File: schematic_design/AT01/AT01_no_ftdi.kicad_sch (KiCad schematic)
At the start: 58 parts, among them J1 JST Connector, J2 Conn_01x08, J3 USB_C_Receptacle_USB2.0, J4 DC Pump Connector, J5 Solenoid Valve Connector, Q1 DMG2301L, Q2 2N7002, Q3 2N7002, SW1 SW_Push, SW2 SW_Push, SW3 SW_Push, U1 MPRLS0025PA00001A, U2 FT232RL, U3 DRV8833PW, U4 MCP73831-2-OT, U5 ESP32-WROOM-32, U6 LM1117MP-3.3

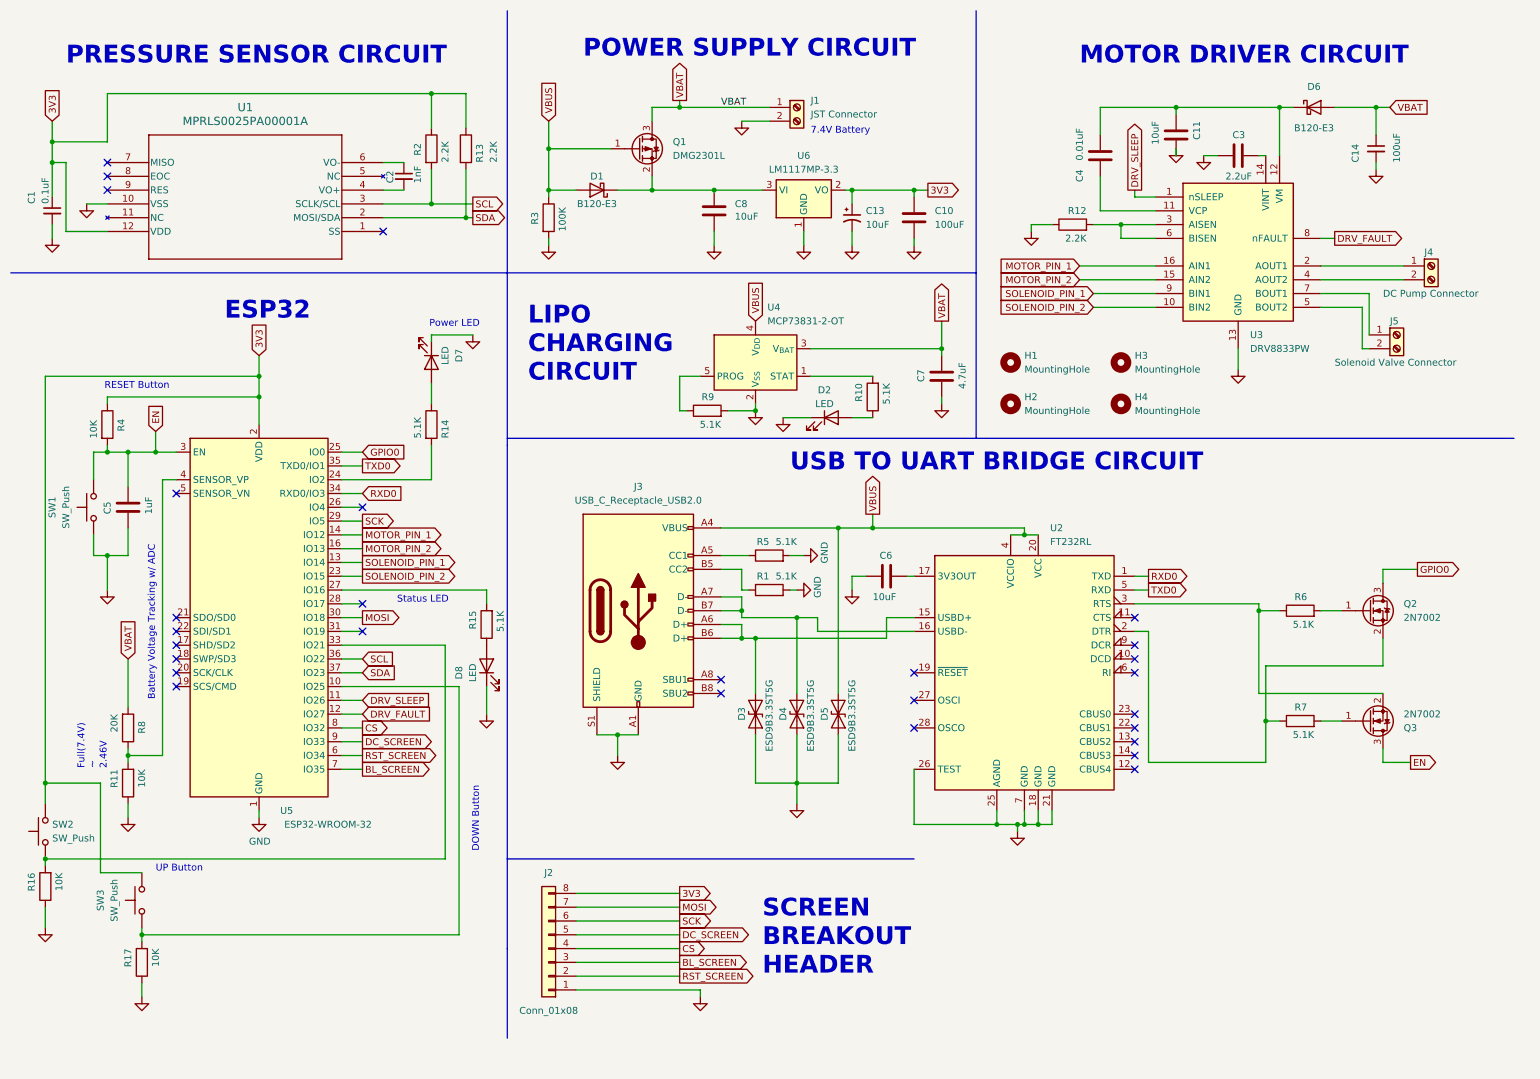
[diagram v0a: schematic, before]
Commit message: adding board with direct USB-C connection, esp32-s3 based
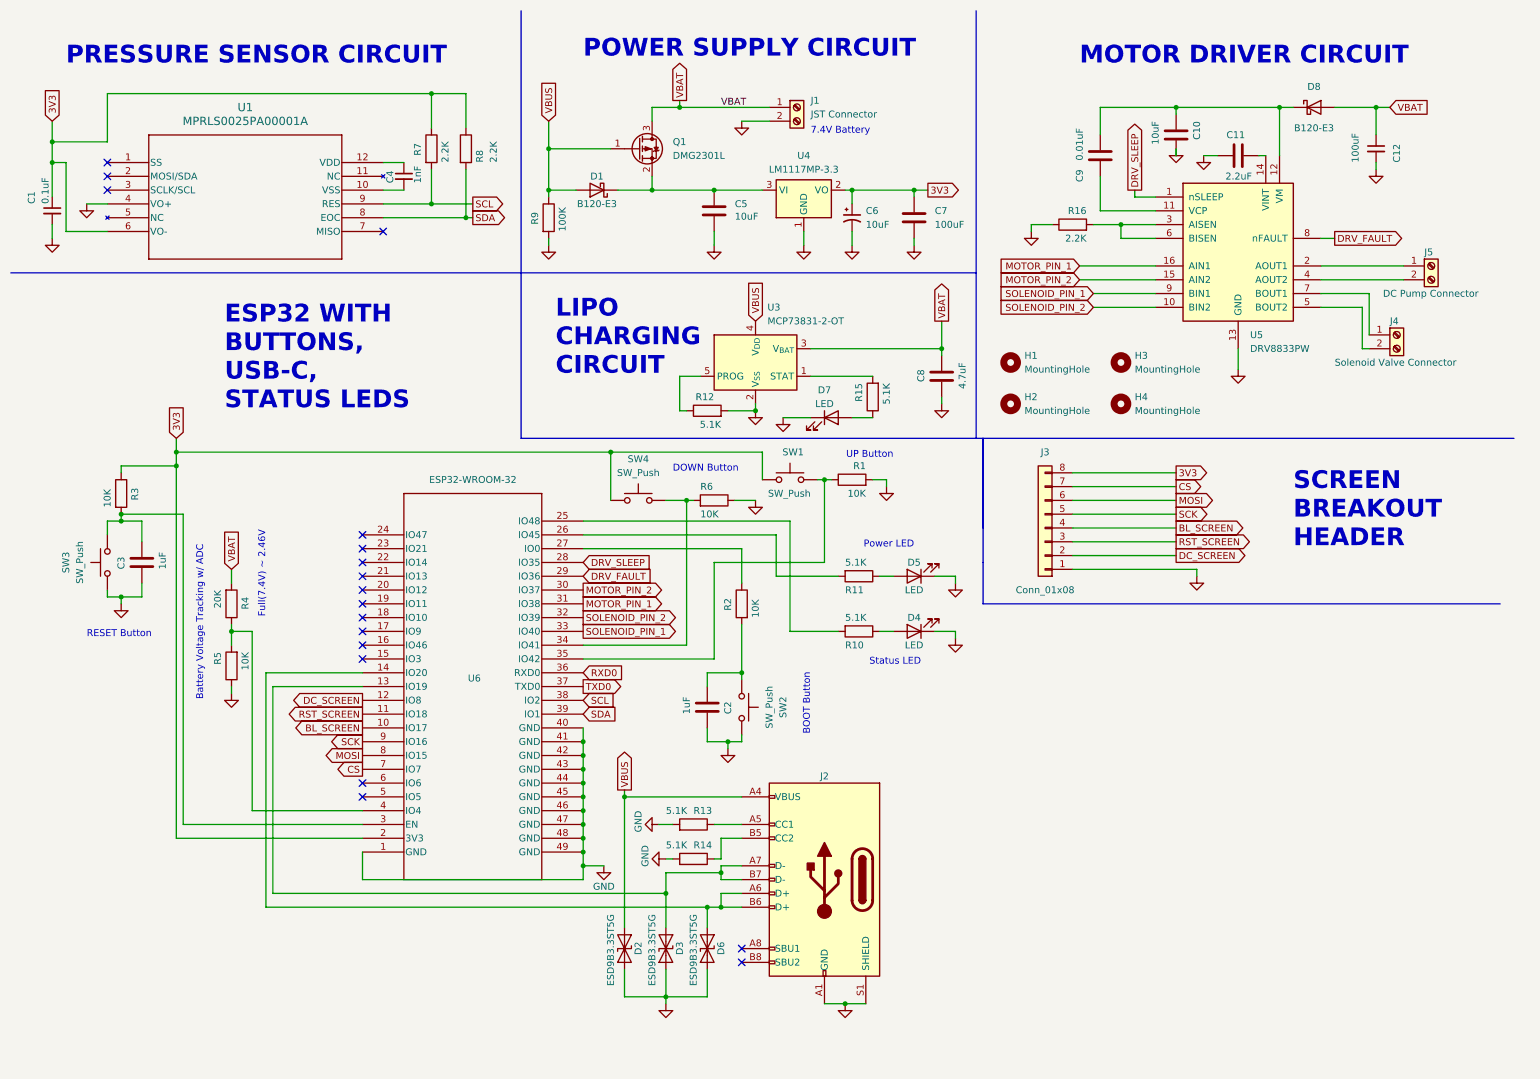
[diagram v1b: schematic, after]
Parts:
- removed C6: 10uF, Capacitor_SMD:C_0402_1005Metric_Pad0.74x0.62mm_HandSolder, symbol Device:C
- removed D4: ESD9B3.3ST5G, Diode_SMD:D_SOD-923, symbol Diode:ESD9B3.3ST5G
- removed D7, D8: LED, LED_THT:LED_D3.0mm, symbol Device:LED
- removed Q2, Q3: 2N7002, Package_TO_SOT_SMD:SOT-23, symbol Transistor_FET:2N7002
- removed R14, R15, R6, R7: 5.1K, Resistor_SMD:R_0402_1005Metric_Pad0.72x0.64mm_HandSolder, symbol Device:R
- removed R16: 10K, Resistor_SMD:R_0402_1005Metric_Pad0.72x0.64mm_HandSolder, symbol Device:R
- removed U2: FT232RL, Package_SO:SSOP-28_5.3x10.2mm_P0.65mm, symbol Interface_USB:FT232RL
- removed U5: ESP32-WROOM-32, RF_Module:ESP32-WROOM-32UE, symbol RF_Module:ESP32-WROOM-32U
- added C2: 1uF, Capacitor_SMD:C_0603_1608Metric_Pad1.08x0.95mm_HandSolder, symbol Device:C
- added D4, D5: LED, LED_THT:LED_D3.0mm, symbol Device:LED
- added D6: ESD9B3.3ST5G, Diode_SMD:D_SOD-923, symbol Diode:ESD9B3.3ST5G
- added R1, R2: 10K, Resistor_SMD:R_0603_1608Metric_Pad0.98x0.95mm_HandSolder, symbol Device:R
- added R10, R11: 5.1K, Resistor_SMD:R_0603_1608Metric_Pad0.98x0.95mm_HandSolder, symbol Device:R
- added SW1: SW_Push, Button_Switch_THT:SW_PUSH_6mm, symbol Switch:SW_Push
- added U6: ESP32-WROOM-32, RF_Module:ESP32-S3-WROOM-1U, symbol 2023-10-27_15-39-09:ESP32-S3-WROOM-1U-N16R8
- C1: footprint Capacitor_SMD:C_0402_1005Metric_Pad0.74x0.62mm_HandSolder -> Capacitor_SMD:C_0603_1608Metric_Pad1.08x0.95mm_HandSolder
- C10: renamed from C11; footprint Capacitor_SMD:C_0402_1005Metric_Pad0.74x0.62mm_HandSolder -> Capacitor_SMD:C_0603_1608Metric_Pad1.08x0.95mm_HandSolder
- C11: renamed from C3; footprint Capacitor_SMD:C_0402_1005Metric_Pad0.74x0.62mm_HandSolder -> Capacitor_SMD:C_0603_1608Metric_Pad1.08x0.95mm_HandSolder
- C12: renamed from C14; footprint Capacitor_SMD:C_0402_1005Metric_Pad0.74x0.62mm_HandSolder -> Capacitor_SMD:C_0603_1608Metric_Pad1.08x0.95mm_HandSolder
- C3: renamed from C5; footprint Capacitor_SMD:C_0402_1005Metric_Pad0.74x0.62mm_HandSolder -> Capacitor_SMD:C_0603_1608Metric_Pad1.08x0.95mm_HandSolder
- C4: renamed from C2; footprint Capacitor_SMD:C_0402_1005Metric_Pad0.74x0.62mm_HandSolder -> Capacitor_SMD:C_0603_1608Metric_Pad1.08x0.95mm_HandSolder
- C5: renamed from C8; footprint Capacitor_SMD:C_0402_1005Metric_Pad0.74x0.62mm_HandSolder -> Capacitor_SMD:C_0603_1608Metric_Pad1.08x0.95mm_HandSolder
- C7: renamed from C10; footprint Capacitor_SMD:C_0402_1005Metric_Pad0.74x0.62mm_HandSolder -> Capacitor_SMD:C_0603_1608Metric_Pad1.08x0.95mm_HandSolder
- C8: renamed from C7; footprint Capacitor_SMD:C_0402_1005Metric_Pad0.74x0.62mm_HandSolder -> Capacitor_SMD:C_0603_1608Metric_Pad1.08x0.95mm_HandSolder
- C9: renamed from C4; footprint Capacitor_SMD:C_0402_1005Metric_Pad0.74x0.62mm_HandSolder -> Capacitor_SMD:C_0603_1608Metric_Pad1.08x0.95mm_HandSolder
- R12: renamed from R9; footprint Resistor_SMD:R_0402_1005Metric_Pad0.72x0.64mm_HandSolder -> Resistor_SMD:R_0603_1608Metric_Pad0.98x0.95mm_HandSolder
- R13: renamed from R5; footprint Resistor_SMD:R_0402_1005Metric_Pad0.72x0.64mm_HandSolder -> Resistor_SMD:R_0603_1608Metric_Pad0.98x0.95mm_HandSolder
- R14: renamed from R1; footprint Resistor_SMD:R_0402_1005Metric_Pad0.72x0.64mm_HandSolder -> Resistor_SMD:R_0603_1608Metric_Pad0.98x0.95mm_HandSolder
- R15: renamed from R10; footprint Resistor_SMD:R_0402_1005Metric_Pad0.72x0.64mm_HandSolder -> Resistor_SMD:R_0603_1608Metric_Pad0.98x0.95mm_HandSolder
- R16: renamed from R12; footprint Resistor_SMD:R_0402_1005Metric_Pad0.72x0.64mm_HandSolder -> Resistor_SMD:R_0603_1608Metric_Pad0.98x0.95mm_HandSolder
- R3: renamed from R4; footprint Resistor_SMD:R_0402_1005Metric_Pad0.72x0.64mm_HandSolder -> Resistor_SMD:R_0603_1608Metric_Pad0.98x0.95mm_HandSolder
- R4: renamed from R8; footprint Resistor_SMD:R_0402_1005Metric_Pad0.72x0.64mm_HandSolder -> Resistor_SMD:R_0603_1608Metric_Pad0.98x0.95mm_HandSolder
- R5: renamed from R11; footprint Resistor_SMD:R_0402_1005Metric_Pad0.72x0.64mm_HandSolder -> Resistor_SMD:R_0603_1608Metric_Pad0.98x0.95mm_HandSolder
- R6: renamed from R17; footprint Resistor_SMD:R_0402_1005Metric_Pad0.72x0.64mm_HandSolder -> Resistor_SMD:R_0603_1608Metric_Pad0.98x0.95mm_HandSolder
- R7: renamed from R2; footprint Resistor_SMD:R_0402_1005Metric_Pad0.72x0.64mm_HandSolder -> Resistor_SMD:R_0603_1608Metric_Pad0.98x0.95mm_HandSolder
- R8: renamed from R13; footprint Resistor_SMD:R_0402_1005Metric_Pad0.72x0.64mm_HandSolder -> Resistor_SMD:R_0603_1608Metric_Pad0.98x0.95mm_HandSolder
- R9: renamed from R3; footprint Resistor_SMD:R_0402_1005Metric_Pad0.72x0.64mm_HandSolder -> Resistor_SMD:R_0603_1608Metric_Pad0.98x0.95mm_HandSolder
- renumbered C13 to C6, D5 to D2, D2 to D7, D6 to D8, J3 to J2, J2 to J3, J5 to J4, J4 to J5, SW1 to SW3, SW3 to SW4, U4 to U3, U6 to U4, U3 to U5
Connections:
- net 3V3: now also U1.6 (VO-), SW1.1, U6.2 (3V3); no longer SW2.1, U1.12 (VDD)
- net BL_SCREEN: now also J3.4 (Pin_4), U6.10 (IO17); no longer J3.3 (Pin_3)
- net CS: now also J3.7 (Pin_7), U6.7 (IO7); no longer J3.4 (Pin_4)
- net DC_SCREEN: now also J3.2 (Pin_2), U6.12 (IO8); no longer J3.5 (Pin_5)
- net DRV_FAULT: now also U6.29 (IO36)
- net DRV_SLEEP: now also U6.28 (IO35)
- net GND: now also SW2.2, U1.4 (VO+), C2.2, D4.1 (K), D5.1 (K), D6.1 (A1), R1.2, U6.1 (GND), U6.40 (GND), U6.41 (GND), U6.42 (GND), U6.43 (GND), U6.44 (GND), U6.45 (GND), U6.46 (GND), U6.47 (GND), U6.48 (GND), U6.49 (GND); no longer U1.10 (VSS)
- net MOSI: now also J3.6 (Pin_6), U6.8 (IO15); no longer J3.7 (Pin_7)
- net MOTOR_PIN_1: now also U6.31 (IO38)
- net MOTOR_PIN_2: now also U6.30 (IO37)
- net RST_SCREEN: now also J3.3 (Pin_3), U6.11 (IO18); no longer J3.2 (Pin_2)
- net RXD0: now also U6.36 (RXD0)
- net SCK: now also J3.5 (Pin_5), U6.9 (IO16); no longer J3.6 (Pin_6)
- net SCL: now also U1.9 (RES), U6.38 (IO2); no longer U1.3 (SCLK/SCL)
- net SDA: now also U1.8 (EOC), U6.39 (IO1); no longer U1.2 (MOSI/SDA)
- net SOLENOID_PIN_1: now also U6.33 (IO40)
- net SOLENOID_PIN_2: now also U6.32 (IO39)
- net TXD0: now also U6.37 (TXD0)
- net at R6.2, SW4.2: now also U6.34 (IO41)
- net at R4.1, R5.2: now also U6.4 (IO4)
- net at J2.A6 (D+), J2.B6 (D+): now also D6.2 (A2), U6.14 (IO20); no longer D3.2 (A2)
- net at J2.A7 (D-), J2.B7 (D-): now also D3.2 (A2), U6.13 (IO19)
- net at C4.1: now also U1.12 (VDD); no longer U1.6 (VO-)
- net at C4.2: now also U1.10 (VSS); no longer U1.4 (VO+)
- net EN: no longer names the net of C3.1, R3.2, SW3.1
- net EN: now also U6.3 (EN)
- new net: R1.1, SW1.2, U6.35 (IO42)
- new net: R10.2, U6.25 (IO48)
- new net: R11.2, U6.26 (IO45)
- new net: R2.1, U6.27 (IO0)
- new net: D4.2 (A), R10.1
- new net: D5.2 (A), R11.1
- new net: C2.1, R2.2, SW2.1
- no-connect marks 28 -> 18
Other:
- note added: "BOOT Button"
- note added: "ESP32 WITH BUTTONS, USB-C, STATUS LEDS"
- note removed: "ESP32"
- note removed: "USB TO UART BRIDGE CIRCUIT"
- moved on the sheet: C3, D2, J2, J3, R13, R14, R3, R4, R5, R6, SW3, SW4

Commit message: added redesigned charging circuit
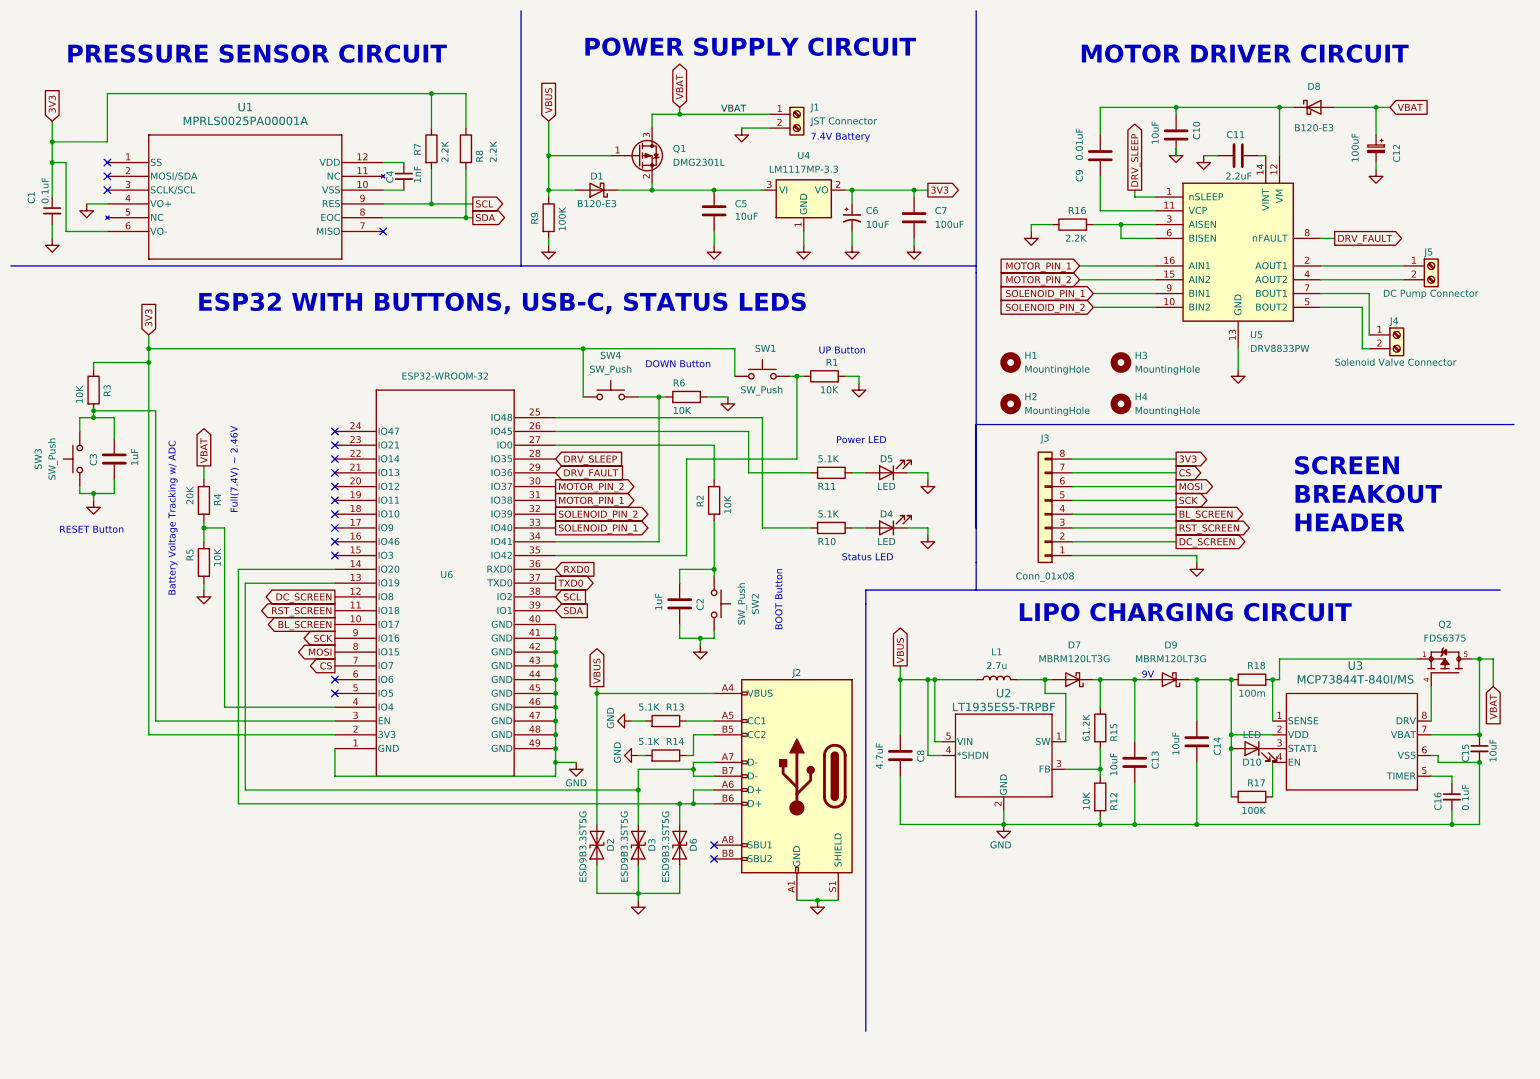
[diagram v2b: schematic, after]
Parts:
- removed D7: LED, LED_THT:LED_D3.0mm, symbol Device:LED
- removed U3: MCP73831-2-OT, Package_TO_SOT_SMD:SOT-23-5, symbol Battery_Management:MCP73831-2-OT
- added C13, C14: 10uF, Capacitor_SMD:C_0603_1608Metric_Pad1.08x0.95mm_HandSolder, symbol Device:C
- added C15: 10uF, Capacitor_SMD:C_0603_1608Metric_Pad1.08x0.95mm_HandSolder, symbol Device:C_Small
- added C16: 0.1uF, Capacitor_SMD:C_0603_1608Metric_Pad1.08x0.95mm_HandSolder, symbol Device:C_Small
- added D10: LED, LED_THT:LED_D3.0mm, symbol Device:LED
- added D7, D9: MBRM120LT3G, Diode_SMD:D_SOD-123F, symbol Diode:MBR1020VL
- added L1: 2.7u, symbol Device:L
- added Q2: FDS6375, FDS6375:SOIC127P600X175-8N, symbol FDS6375:FDS6375
- added R17: 100K, Resistor_SMD:R_0603_1608Metric_Pad0.98x0.95mm_HandSolder, symbol Device:R
- added R18: 100m, Resistor_SMD:R_0603_1608Metric_Pad0.98x0.95mm_HandSolder, symbol Device:R
- added U2: LT1935ES5-TRPBF, S_5_ADI, symbol 2023-10-27_15-39-09:LT1935ES5-TRPBF
- added U3: MCP73844T-840I/MS, MSOP8_MC_MCH, symbol 2023-10-27_15-39-09:MCP73844T-840I_MS
- C12: footprint Capacitor_SMD:C_0603_1608Metric_Pad1.08x0.95mm_HandSolder -> Capacitor_SMD:CP_Elec_6.3x5.2; symbol Device:C_Small -> Device:C_Polarized_Small
- J4, J5: footprint Connector_JST:JST_EH_S2B-EH_1x02_P2.50mm_Horizontal -> TerminalBlock:TerminalBlock_Altech_AK300-2_P5.00mm
- R12: value 5.1K -> 10K
- R15: value 5.1K -> 61.2K; footprint Resistor_SMD:R_0603_1608Metric_Pad0.98x0.95mm_HandSolder -> Resistor_SMD:R_0402_1005Metric_Pad0.72x0.64mm_HandSolder
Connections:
- net GND: now also C8.2, C13.2, C14.2, C15.2, C16.2, U2.2 (GND), U3.6 (VSS); no longer C8.1
- net VBAT: now also C15.1, Q2.5, U3.7 (VBAT); no longer C8.2
- net VBUS: now also C8.1, L1.1, U2.4 (*SHDN), U2.5 (VIN)
- net at R15.1: now also C13.1, D7.1 (K), D9.2 (A)
- net at R15.2: now also R12.1, U2.3 (FB)
- new net: Q2.1, R18.2, U3.1 (SENSE)
- new net: C14.1, D10.2 (A), D9.1 (K), R17.1, R18.1, U3.2 (VDD)
- new net: D10.1 (K), U3.3 (STAT1)
- new net: R17.2, U3.4 (EN)
- new net: C16.1, U3.5 (TIMER)
- new net: Q2.4, U3.8 (DRV)
- new net: D7.2 (A), L1.2, U2.1 (SW)
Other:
- note added: "9V"
- moved on the sheet: C2, C3, D2, D3, D4, D5, D6, J1, J2, J3, Q1, R1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
